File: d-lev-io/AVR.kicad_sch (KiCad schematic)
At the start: 10 parts, among them J7 PROG_HDR, U1 ATmega32U4-M, Y1 16Mhz

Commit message: more minor pusharounds and updates
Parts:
- C1, C2, C3, C4, C5: footprint (none) -> Capacitor_SMD:C_0603_1608Metric
- R8, R9: footprint (none) -> Resistor_SMD:R_0603_1608Metric
- Y1: footprint (none) -> Oscillator:Oscillator_SMD_Abracon_ASE-4Pin_3.2x2.5mm
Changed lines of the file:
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@@
       (effects (font (size 1.27 1.27)) (justify right))
     )
-    (property "Footprint" "" (at 118.11 80.645 0)
+    (property "Footprint" "Capacitor_SMD:C_0603_1608Metric" (at 118.11 80.645 0)
       (effects (font (size 1.27 1.27)) hide)
     )
@@
       (effects (font (size 1.27 1.27)))
     )
-    (property "Footprint" "" (at 130.81 88.9 0)
+    (property "Footprint" "Capacitor_SMD:C_0603_1608Metric" (at 130.81 88.9 0)
       (effects (font (size 1.27 1.27)) hide)
     )
@@
       (effects (font (size 1.27 1.27)) (justify right))
     )
-    (property "Footprint" "" (at 191.77 114.935 0)
+    (property "Footprint" "Resistor_SMD:R_0603_1608Metric" (at 191.77 114.935 0)
       (effects (font (size 1.27 1.27)) hide)
     )
@@
       (effects (font (size 1.27 1.27)))
     )
-    (property "Footprint" "" (at 113.665 67.31 0)
+    (property "Footprint" "Capacitor_SMD:C_0603_1608Metric" (at 113.665 67.31 0)
       (effects (font (size 1.27 1.27)) hide)
     )
@@
       (effects (font (size 1.27 1.27)) (justify right))
     )
-    (property "Footprint" "" (at 121.92 62.865 0)
+    (property "Footprint" "Oscillator:Oscillator_SMD_Abracon_ASE-4Pin_3.2x2.5mm" (at 121.92 62.865 0)
       (effects (font (size 1.27 1.27)) hide)
     )
@@
       (effects (font (size 1.27 1.27)))
     )
-    (property "Footprint" "" (at 113.665 59.055 0)
+    (property "Footprint" "Capacitor_SMD:C_0603_1608Metric" (at 113.665 59.055 0)
       (effects (font (size 1.27 1.27)) hide)
     )
@@
       (effects (font (size 1.27 1.27)))
     )
-    (property "Footprint" "" (at 160.02 43.815 0)
+    (property "Footprint" "Capacitor_SMD:C_0603_1608Metric" (at 160.02 43.815 0)
       (effects (font (size 1.27 1.27)) hide)
     )
@@
       (effects (font (size 1.27 1.27)) (justify right))
     )
-    (property "Footprint" "" (at 128.905 50.165 0)
-      (effects (font (size 1.27 1.27)) hide)
-    )
+    (property "Footprint" "Resistor_SMD:R_0603_1608Metric" (at 128.905 50.165 0)
+      (effects (font (size 1.27 1.27)) hide)
+    )

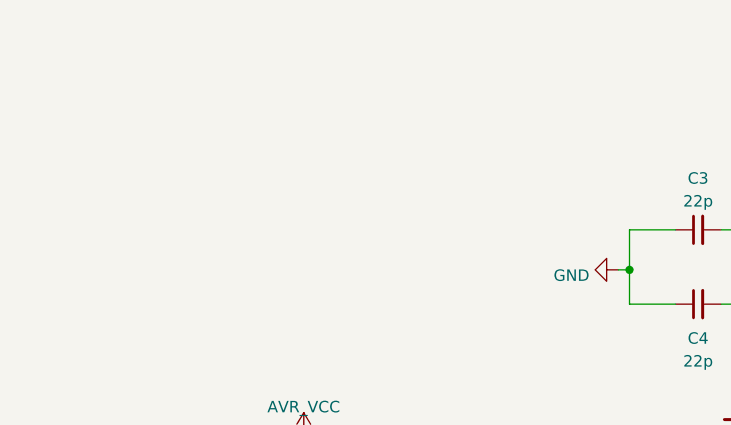
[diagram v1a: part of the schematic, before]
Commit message: Improve routing and rearrange I/O connector
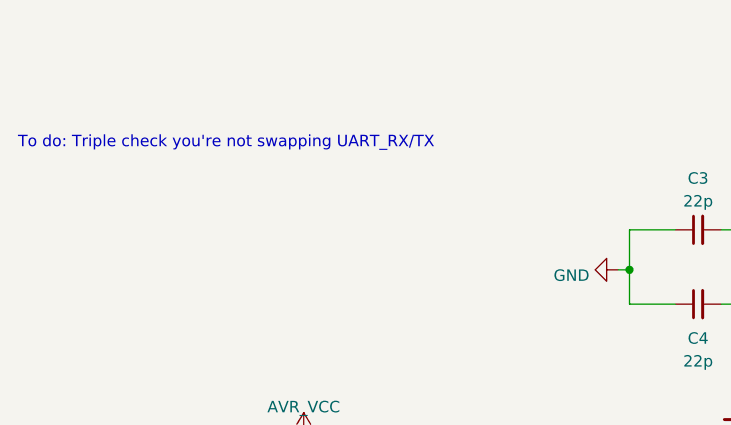
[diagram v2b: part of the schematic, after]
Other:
- note added: "To do: Triple check you're not swapping UART_RX/TX"
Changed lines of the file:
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@@
     (stroke (width 0) (type default))
+  )
+  (text "To do: Triple check you're not swapping UART_RX/TX"
+    (at 38.1 50.165 0)
+    (effects (font (size 1.27 1.27)) (justify left bottom))
   )
   (label "ICSP.SCK" (at 208.915 88.9 0) (fields_autoplaced)

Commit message: many many changes'
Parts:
- J7: footprint (none) -> Connector:Tag-Connect_TC2030-IDC-NL_2x03_P1.27mm_Vertical
- Y1: value 16Mhz -> 8MHz
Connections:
- net UART_5V.RX renamed UART_AVR.RX
- net UART_5V.TX renamed UART_AVR.TX
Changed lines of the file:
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@@
     (effects (font (size 1.27 1.27)) (justify right bottom))
   )
-  (label "UART_5V.RX" (at 183.515 96.52 180) (fields_autoplaced)
+  (label "UART_AVR.RX" (at 183.515 96.52 180) (fields_autoplaced)
     (effects (font (size 1.27 1.27)) (justify right bottom))
   )
@@
     (effects (font (size 1.27 1.27)) (justify right bottom))
   )
-  (label "UART_5V.TX" (at 183.515 93.98 180) (fields_autoplaced)
+  (label "UART_AVR.TX" (at 183.515 93.98 180) (fields_autoplaced)
     (effects (font (size 1.27 1.27)) (justify right bottom))
   )
@@
     (effects (font (size 1.27 1.27)) (justify right))
   )
-  (hierarchical_label "UART_5V{RX,TX}" (shape bidirectional) (at 66.04 90.805 180) (fields_autoplaced)
+  (hierarchical_label "UART_AVR{RX,TX}" (shape bidirectional) (at 66.04 90.805 180) (fields_autoplaced)
     (effects (font (size 1.27 1.27)) (justify right))
   )
@@
       (effects (font (size 1.27 1.27)))
     )
-    (property "Footprint" "" (at 231.14 88.9 0)
+    (property "Footprint" "Connector:Tag-Connect_TC2030-IDC-NL_2x03_P1.27mm_Vertical" (at 231.14 88.9 0)
       (effects (font (size 1.27 1.27)) hide)
     )
     (property "Datasheet" "~" (at 231.14 88.9 0)
       (effects (font (size 1.27 1.27)) hide)
+    )
+    (property "Tolerance" "" (at 231.14 88.9 0)
+      (effects (font (size 1.27 1.27)))
     )
     (pin "1")
@@
       (effects (font (size 1.27 1.27)) (justify right))
     )
-    (property "Value" "16Mhz" (at 126.365 64.77 90)
+    (property "Value" "8MHz" (at 126.365 64.77 90)
       (effects (font (size 1.27 1.27)) (justify right))
     )
@@
       (effects (font (size 1.27 1.27)) hide)
     )
-    (pin "1")
+    (property "Tolerance" "" (at 121.92 62.865 0)
+      (effects (font (size 1.27 1.27)))
+    )
+    (pin "1")

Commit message: many more changes
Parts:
- renumbered C5 to C10, C1 to C11, C2 to C12, C3 to C8, C4 to C9, J7 to J5, R9 to R10, R8 to R9
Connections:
- net UART_AVR.RX renamed UART_AVR_RX
- net UART_AVR.TX renamed UART_AVR_TX
- net UART_SOFT.RX renamed UART_AVR_SOFT_RX
- net UART_SOFT.TX renamed UART_AVR_SOFT_TX
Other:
- note added: "To do: add at least three LEDs for debugging"
- moved on the sheet: Y1
